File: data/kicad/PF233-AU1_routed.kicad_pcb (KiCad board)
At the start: 6 copper layers, 36 x 44 mm, 51 parts

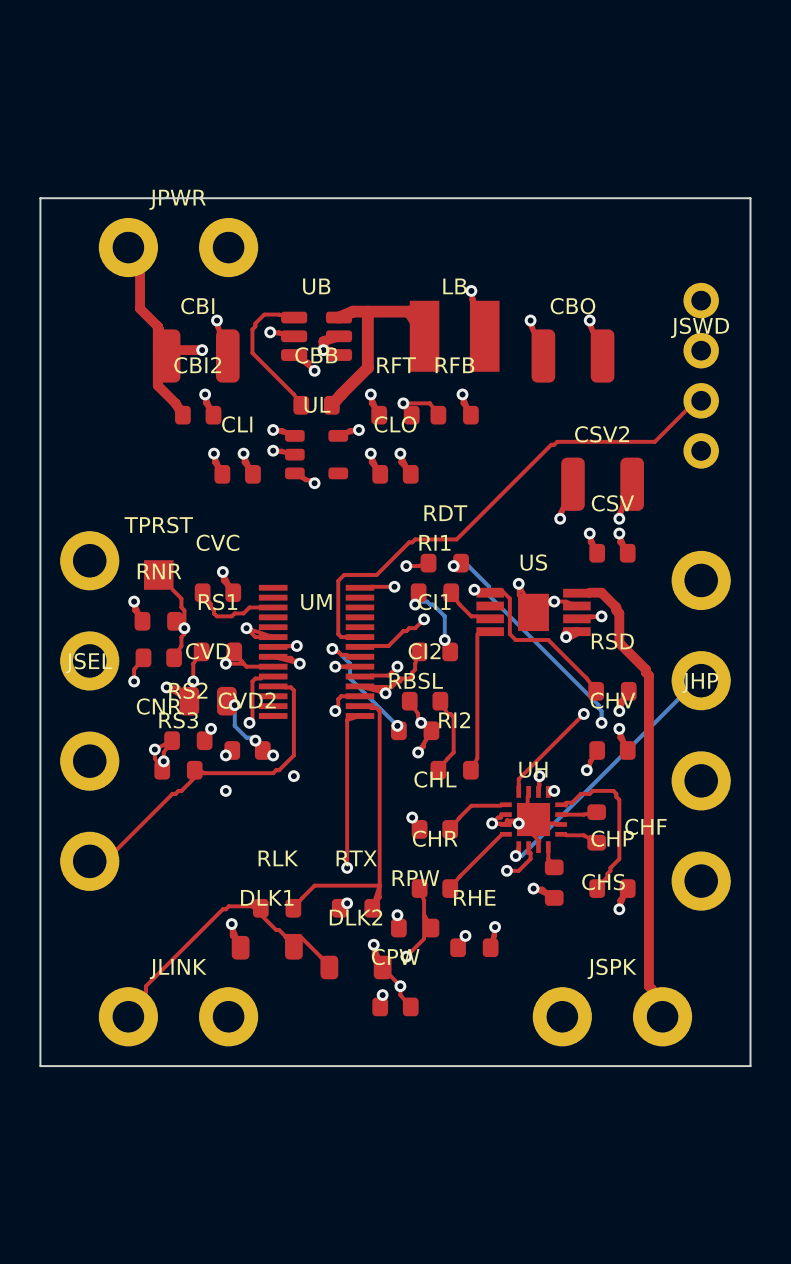
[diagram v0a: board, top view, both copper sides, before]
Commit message: WIP (NOT signed off): data published by the second close-out run (8 FAIL: 3 opens on CB1D-C2 / AU1 under the exact fine-zone keep-out); third run in progress
Co-Authored-By: Claude Opus 5.5 <noreply@anthropic.com>
Claude-Session: https://claude.ai/code/session_01FX4DWSYYjMCFGGA6gmha65
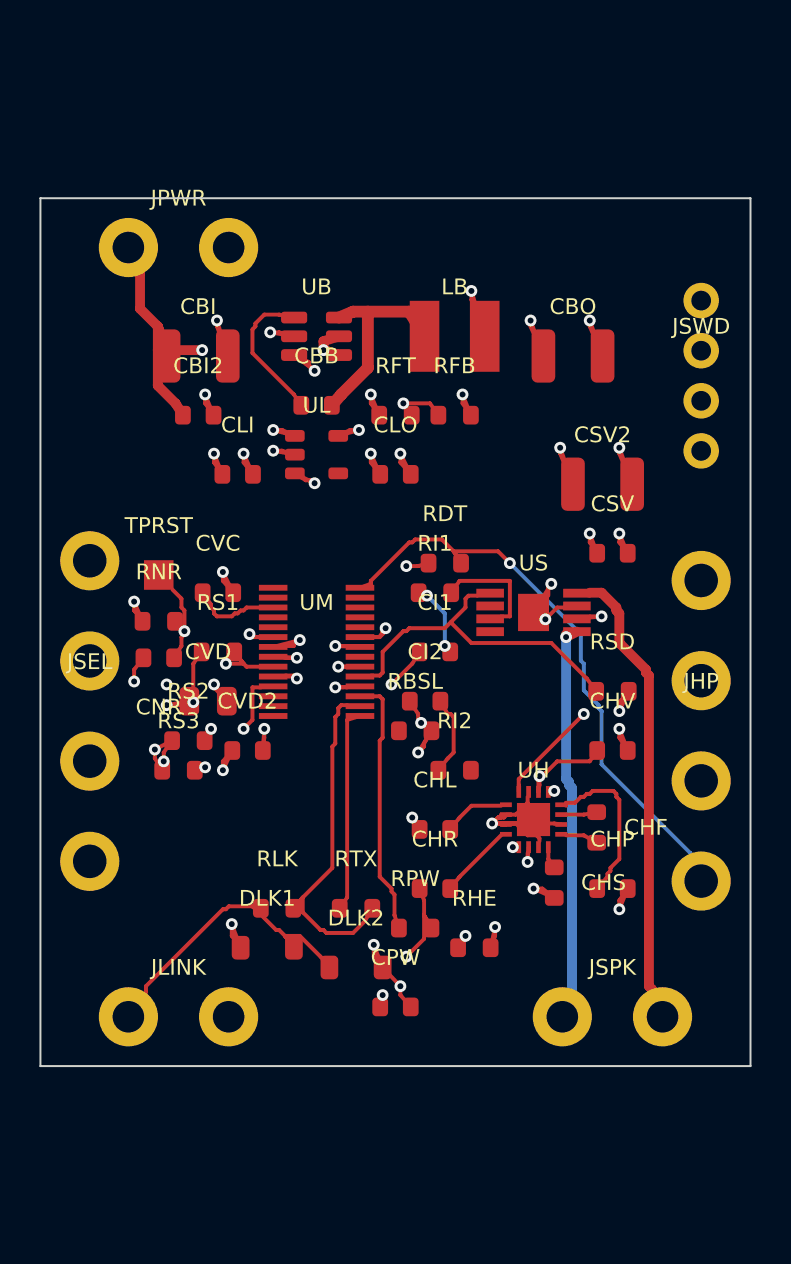
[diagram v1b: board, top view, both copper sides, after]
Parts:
- removed the JSWD at (115.5, 87.0)
- added JSWD: SWD: 3V3 SWDIO SWCLK GND, Connector:Wire_pads_1x4_P2.54mm, F.Cu at (115.5, 87.0)
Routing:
- net US_INN: track 6.98 -> 0.00 mm
- net BSL_INV: track 6.23 -> 0.00 mm, vias 2 -> 0
- net GND: track 74.6 -> 80.8 mm, vias 30 -> 28
- net HP_DET: track 26.7 -> 30.6 mm, vias 3 -> 1
- net US_INP: track 1.88 -> 5.54 mm
- net SWDIO_AU: track 22.9 -> 26.5 mm
- net SEL3: track 17.4 -> 14.3 mm, vias 0 -> 2
- net SEL2: track 12.8 -> 15.4 mm
- net +3V3_AU: track 28.8 -> 31.0 mm, vias 15 -> 13
- net SWCLK_AU: track 25.3 -> 23.3 mm, vias 0 -> 1
- net SPK_INP: track 5.64 -> 3.82 mm
- net PWM_AU: track 14.1 -> 12.7 mm, vias 2 -> 0
- net LINK_N: track 16.7 -> 17.6 mm
- net SPK_SD: track 17.3 -> 16.8 mm, vias 2 -> 0
- net LINK_TX: track 9.98 -> 10.3 mm, vias 2 -> 0
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
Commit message: WIP (NOT signed off): data written by the close-out runs in progress (fourth run with the 0.15 mm fine-pitch neck-down is running)
Co-Authored-By: Claude Opus 5.5 <noreply@anthropic.com>
Claude-Session: https://claude.ai/code/session_01FX4DWSYYjMCFGGA6gmha65
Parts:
- moved RI2 7.12 mm to (102.0, 100.0)
- moved CI1 0.80 mm to (102.0, 101.8)
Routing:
- net HP_EN: track 26.0 -> 0.00 mm, vias 3 -> 0
- net LINK_N: track 17.6 -> 0.00 mm
- net PWM_AU: track 12.7 -> 0.00 mm
- net GND: track 80.8 -> 72.0 mm, vias 28 -> 31
- net SPK_SD: track 16.8 -> 21.5 mm, vias 0 -> 2
- net BSL_INV: track 0.00 -> 4.55 mm
- net SPK_INN: track 4.10 -> 8.40 mm, vias 0 -> 2
- net US_INP: track 5.54 -> 1.97 mm
- net SPK_INP: track 3.82 -> 6.27 mm
- net DAC_AU: track 15.5 -> 17.7 mm, vias 3 -> 2
- net SWCLK_AU: track 23.3 -> 21.7 mm
- net US_INN: track 0.00 -> 1.33 mm
- net LINK_TX: track 10.3 -> 10.8 mm, vias 0 -> 2

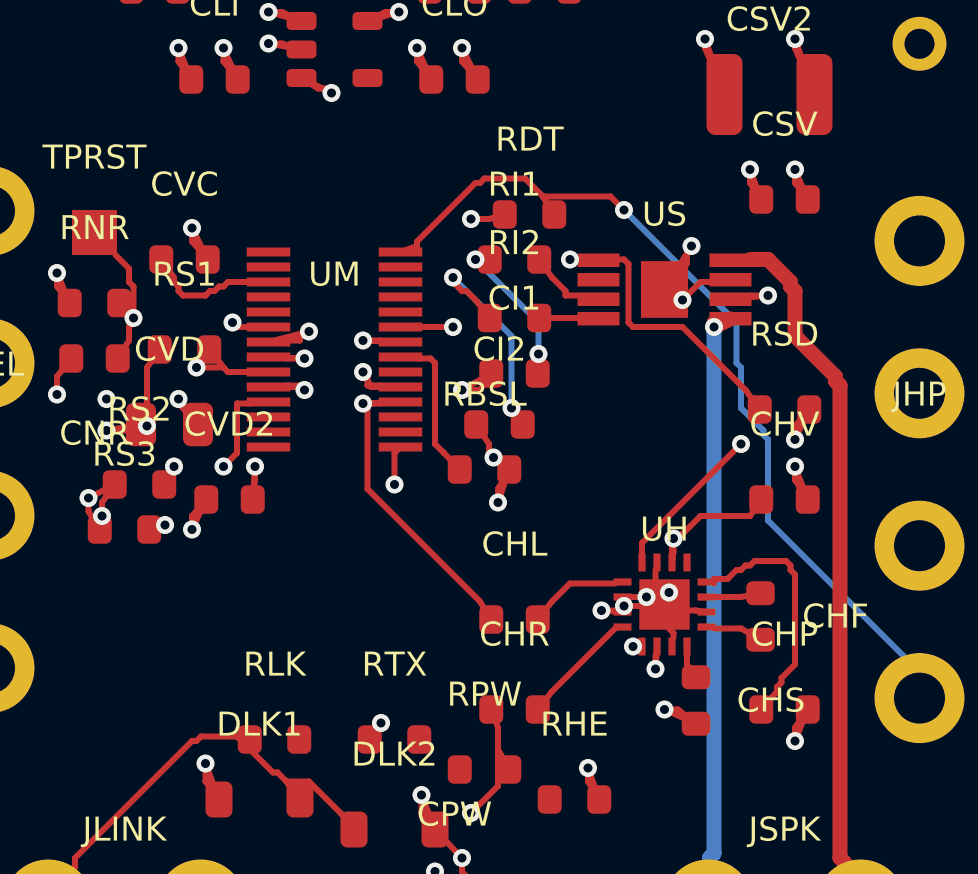
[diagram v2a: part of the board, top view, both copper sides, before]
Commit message: WIP: per-board 0.125 mm routing grid for AU1 / CB1D (0.5 mm-pitch rows on grid lines); fine zone radius in mm; AU1 route on the new grid running
Co-Authored-By: Claude Opus 5.5 <noreply@anthropic.com>
Claude-Session: https://claude.ai/code/session_01FX4DWSYYjMCFGGA6gmha65
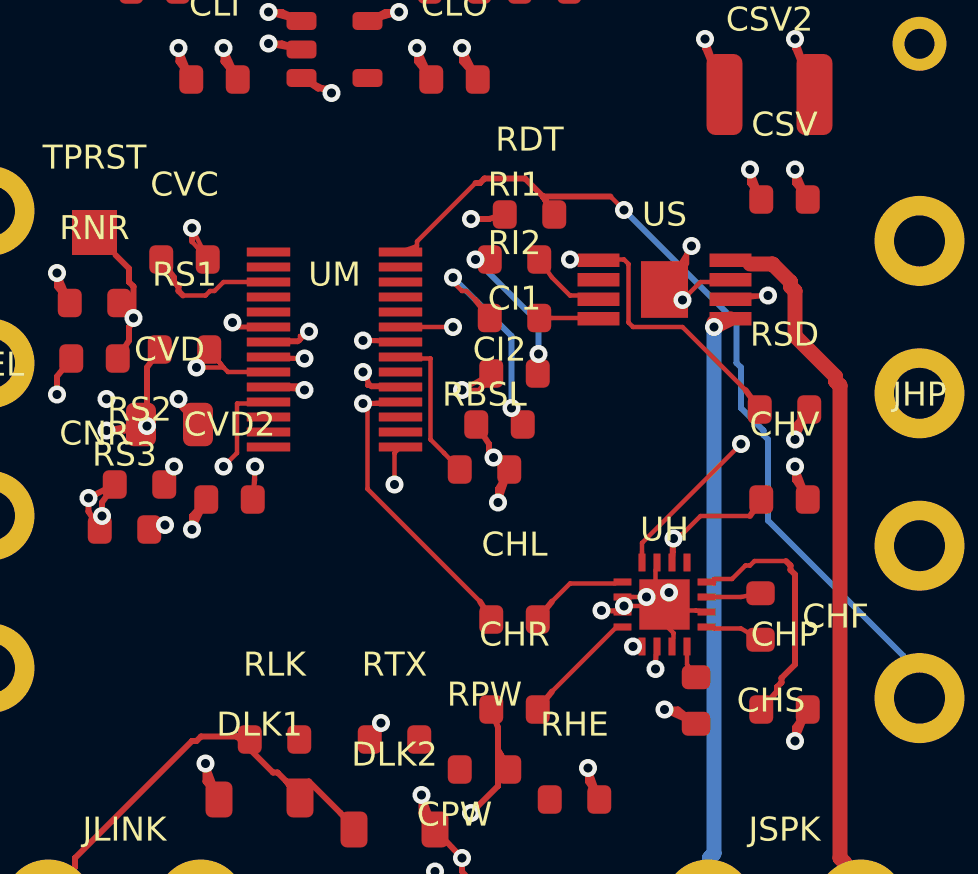
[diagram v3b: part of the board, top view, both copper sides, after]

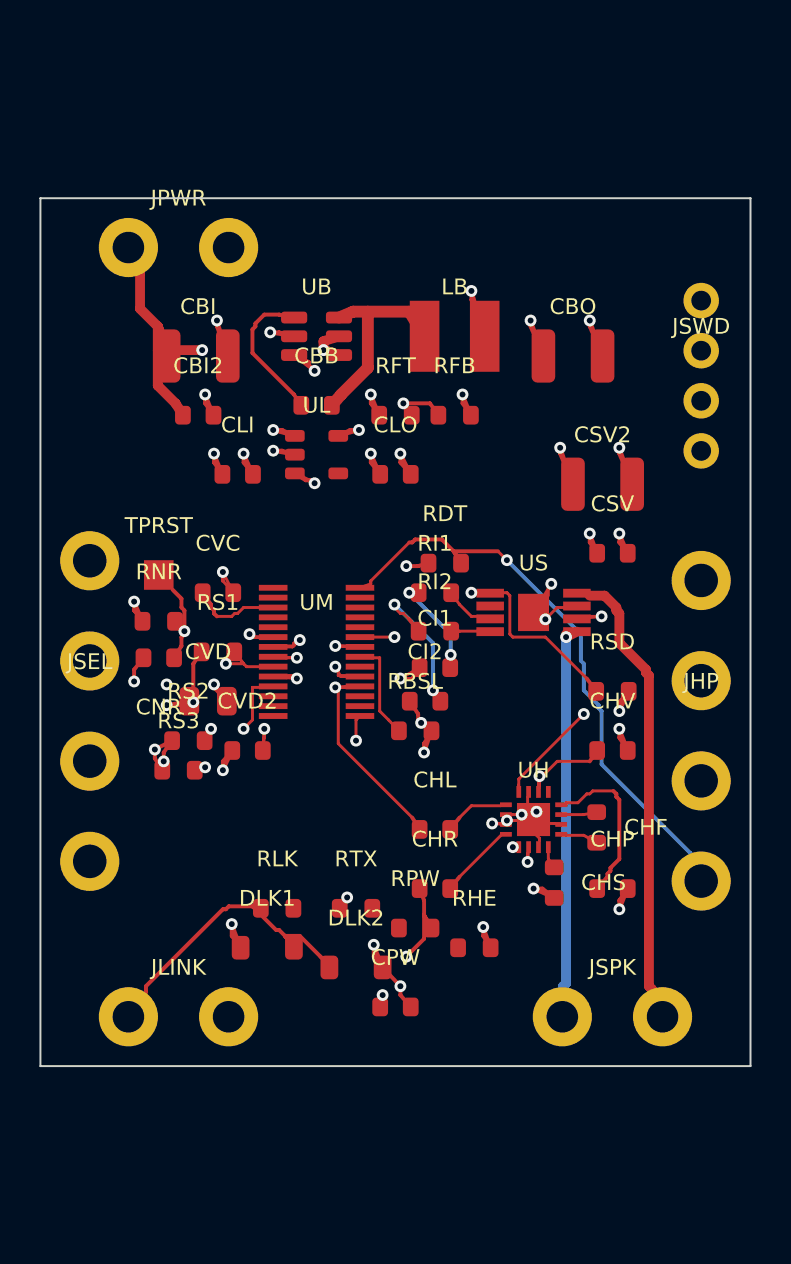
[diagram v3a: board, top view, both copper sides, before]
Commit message: WIP (NOT signed off): sign-off outputs with AU1 38 / 38 (exact DRC 0 / 0, all AU1 checks pass); CB1D 45 / 46 (TRIG_EXT open on the 0.125 grid, being re-routed on 0.15)
Co-Authored-By: Claude Opus 5.5 <noreply@anthropic.com>
Claude-Session: https://claude.ai/code/session_01FX4DWSYYjMCFGGA6gmha65
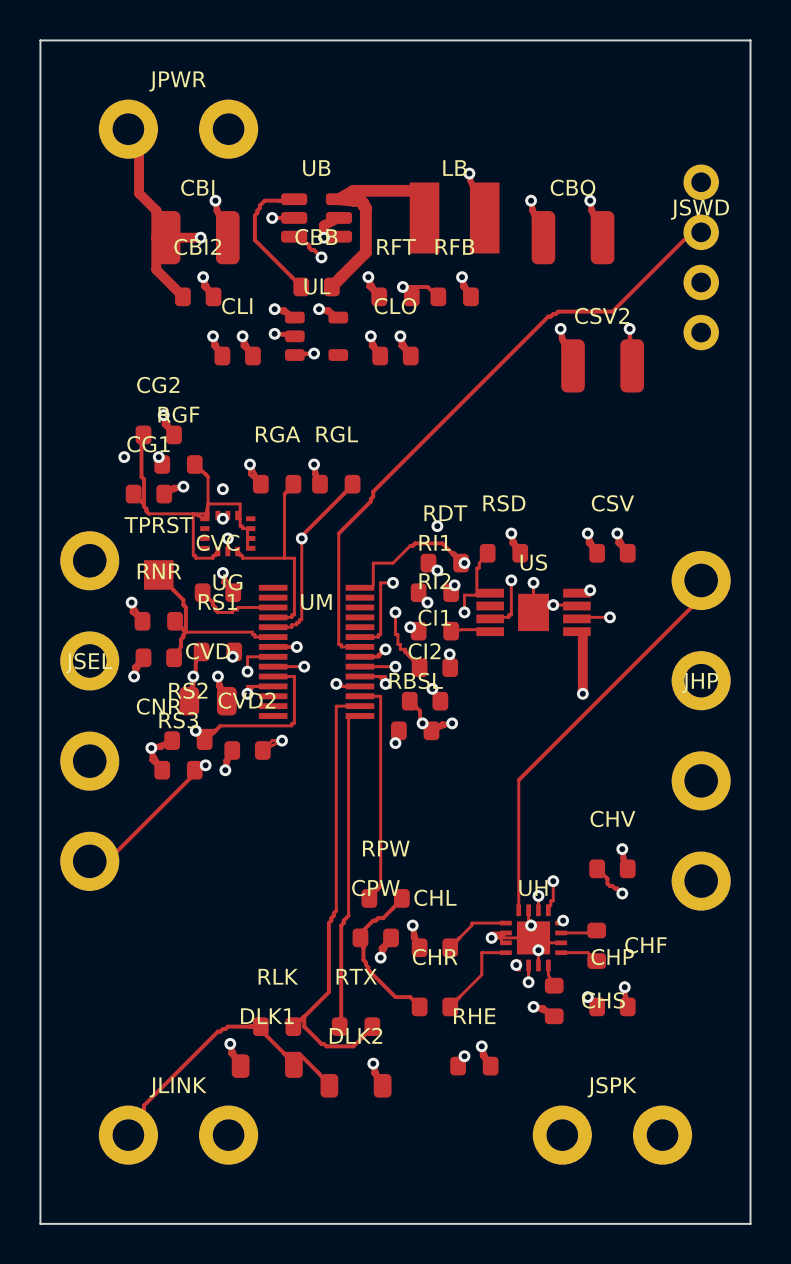
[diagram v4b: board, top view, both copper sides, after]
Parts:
- added CG1: 100n, Capacitor_SMD:C_0603_1608Metric, F.Cu at (87.5, 93.0)
- added CG2: 100n, Capacitor_SMD:C_0603_1608Metric, F.Cu at (88.0, 90.0)
- added RGA: 4k7, Resistor_SMD:R_0603_1608Metric, F.Cu at (94.0, 92.5)
- added RGF: 10R, Resistor_SMD:R_0603_1608Metric, F.Cu at (89.0, 91.5)
- added RGL: 4k7, Resistor_SMD:R_0603_1608Metric, F.Cu at (97.0, 92.5)
- added UG: BMI270, PF233:BMI270_LGA-14_2.5x3.0mm, F.Cu at (91.5, 95.0)
- moved RSD 8.90 mm to (105.5, 96.0)
- moved CBB 6.00 mm to (96.0, 82.5)
- moved CBI 6.00 mm to (90.0, 80.0)
- moved CBI2 6.00 mm to (90.0, 83.0)
- moved CBO 6.00 mm to (109.0, 80.0)
- moved CHF 6.00 mm to (110.2, 115.9)
- moved CHL 6.00 mm to (102.0, 116.0)
- moved CHP 6.00 mm to (111.0, 119.0)
- moved CHR 6.00 mm to (102.0, 119.0)
- moved CHS 6.00 mm to (108.0, 118.7)
- moved CHV 6.00 mm to (111.0, 112.0)
- moved CLI 6.00 mm to (92.0, 86.0)
- moved CLO 6.00 mm to (100.0, 86.0)
- moved CSV2 6.00 mm to (110.5, 86.5)
- moved DLK1 6.00 mm to (93.5, 122.0)
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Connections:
- UM pad 4: UM_P4_NC -> GYR_SDA
- UM pad 5: UM_P5_NC -> GYR_SCL
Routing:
- net HP_EN: track 0.00 -> 30.0 mm, vias 0 -> 3
- net LINK_N: track 0.00 -> 23.3 mm
- net UG_VIO: track 0.00 -> 21.0 mm
- net GYR_SCL: track 0.00 -> 14.1 mm, vias 0 -> 2
- net PWM_AU: track 0.00 -> 10.8 mm
- net DAC_AU: track 17.7 -> 28.5 mm, vias 2 -> 3
- net GYR_SDA: track 0.00 -> 10.4 mm
- net SPK_SD: track 21.5 -> 12.7 mm
- net +3V3_AU: track 31.1 -> 37.8 mm, vias 13 -> 17
- net GND: track 72.0 -> 77.9 mm, vias 31 -> 33
- net SPK_P: track 20.1 -> 25.9 mm
- net SPK_N: track 23.2 -> 29.0 mm, vias 0 -> 1
- net HP_L: track 14.4 -> 20.2 mm, vias 1 -> 0
- net BSL_INV: track 4.55 -> 9.87 mm, vias 0 -> 2
- net LINK_TX: track 10.8 -> 15.8 mm, vias 2 -> 0
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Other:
- board size 36 x 44 mm -> 36 x 60 mm
- copper layers 6 -> 8

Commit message: WIP: sign-off outputs (75 / 1 before the process-guard fix; deadline test and re-run in progress)
Co-Authored-By: Claude Opus 5.5 <noreply@anthropic.com>
Claude-Session: https://claude.ai/code/session_01FX4DWSYYjMCFGGA6gmha65
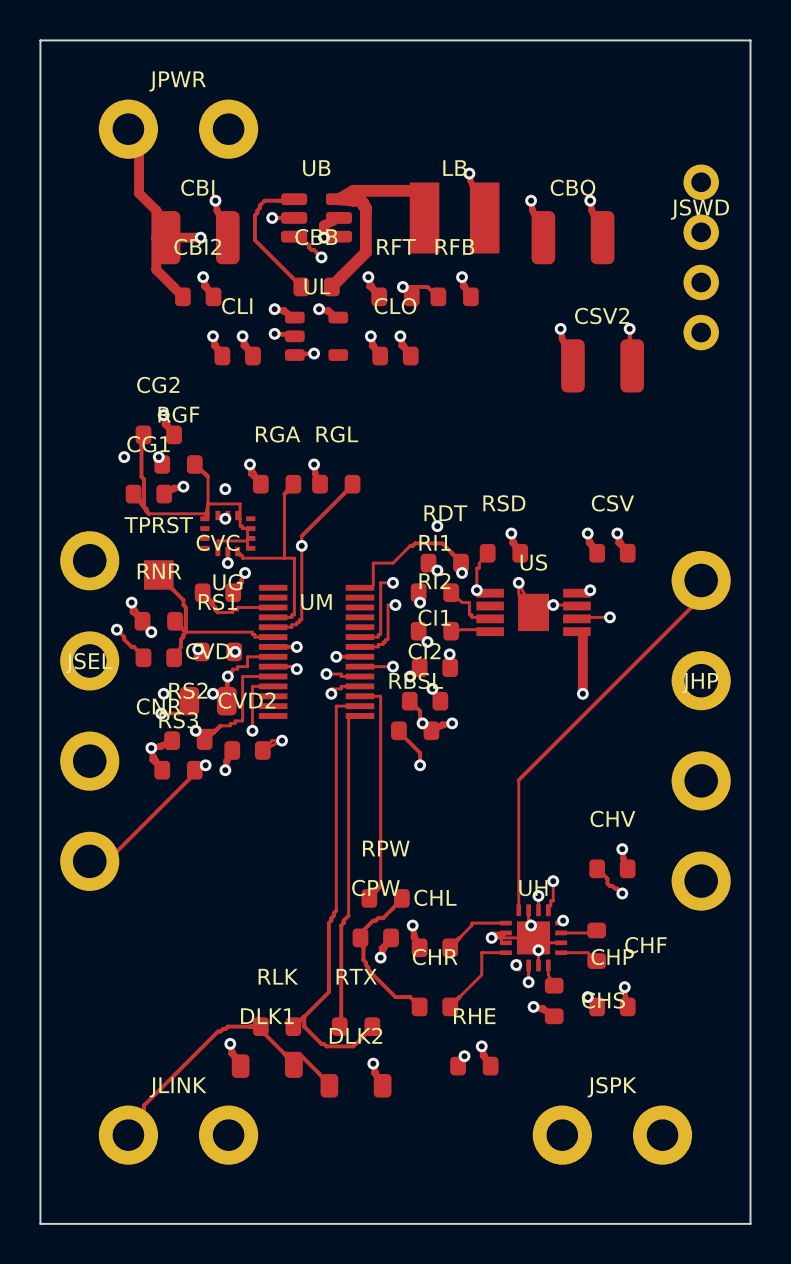
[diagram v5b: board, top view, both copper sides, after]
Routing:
- net GND: track 77.9 -> 85.2 mm, vias 33 -> 34
- net DAC_AU: track 28.5 -> 21.7 mm
- net HP_DET: track 29.6 -> 34.2 mm
- net BSL_INV: track 9.87 -> 14.4 mm
- net US_INP: track 5.50 -> 2.24 mm, vias 2 -> 0
- net HP_R: track 18.4 -> 21.4 mm
- net +3V3_AU: track 37.8 -> 40.6 mm, vias 17 -> 19
- net VCORE_AU: track 3.70 -> 6.23 mm
- net SWDIO_AU: track 31.1 -> 28.7 mm, vias 0 -> 1
- net UG_VIO: track 21.0 -> 23.0 mm
- net SWCLK_AU: track 25.7 -> 27.6 mm
- net PWM_AU: track 10.8 -> 12.5 mm
- net NRST_AU: track 11.3 -> 12.9 mm
- net SEL3: track 16.9 -> 15.5 mm
- net HP_INR: track 4.41 -> 5.78 mm
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
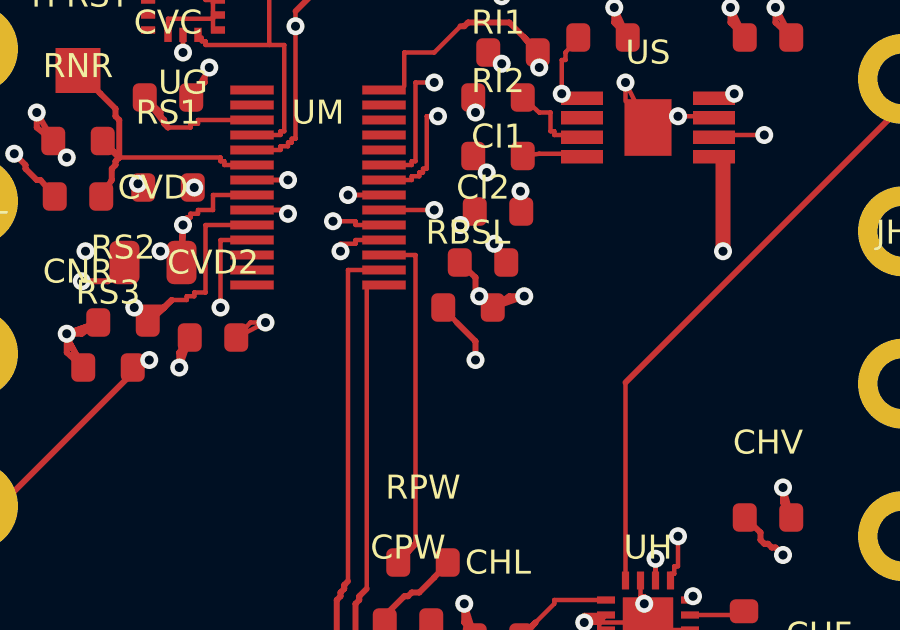
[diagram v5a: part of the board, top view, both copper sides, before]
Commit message: Controls step writes a fresh board table first (stale regress / controls rows had made the release refusals misfire); handoff updated: sign-off 76 / 0 / 4, strict regress 115 / 0, controls 12 / 12, publish 0 stale
Co-Authored-By: Claude Opus 5.5 <noreply@anthropic.com>
Claude-Session: https://claude.ai/code/session_01FX4DWSYYjMCFGGA6gmha65
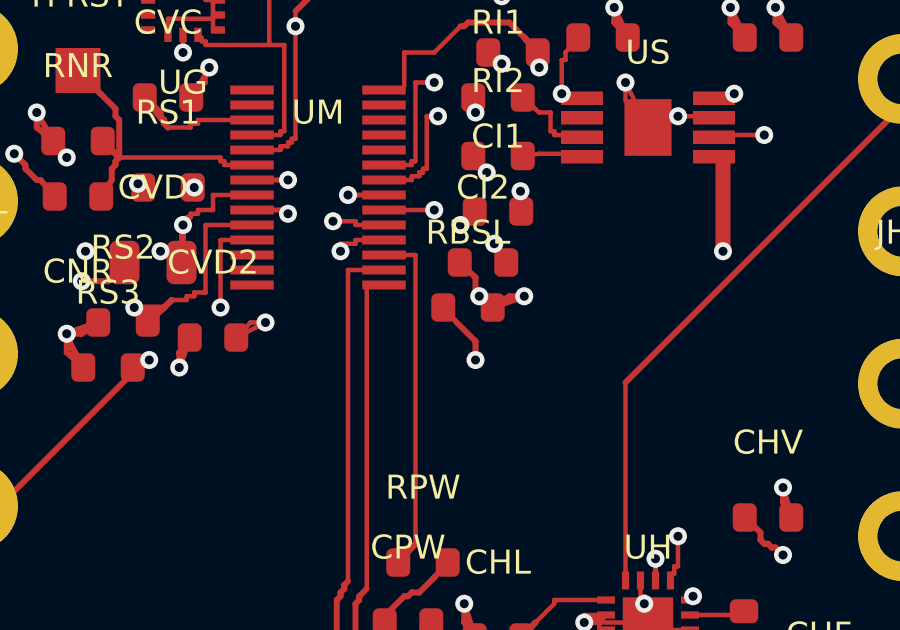
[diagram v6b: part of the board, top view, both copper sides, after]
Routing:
- net BSL_INV: track 14.4 -> 15.7 mm
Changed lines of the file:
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@@
+  (segment (start 100.1750 105.0000) (end 100.6250 105.5000) (width 0.15) (layer "F.Cu") (net 4))
+  (segment (start 100.6250 105.5000) (end 100.1750 105.0000) (width 0.15) (layer "F.Cu") (net 4))
   (segment (start 100.1750 105.0000) (end 100.6250 105.5000) (width 0.15) (layer "F.Cu") (net 4))
   (segment (start 100.6250 105.5000) (end 100.1750 105.0000) (width 0.15) (layer "F.Cu") (net 4))
